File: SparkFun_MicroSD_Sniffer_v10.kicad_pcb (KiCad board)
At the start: 16 copper layers, 47 x 27.9 mm, 9 parts, among them U1 MICRO-SDCARD

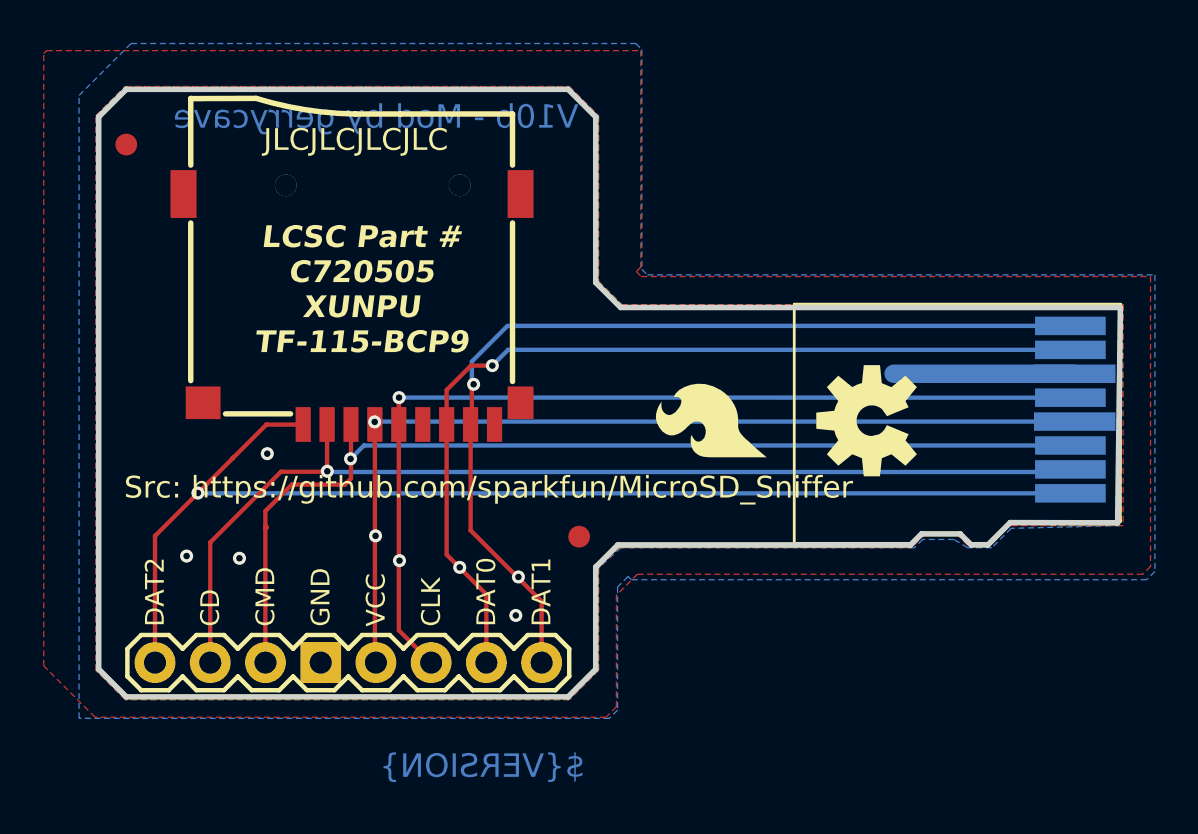
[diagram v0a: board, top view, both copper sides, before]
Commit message: Add silkscreen to increase height in the uSD section
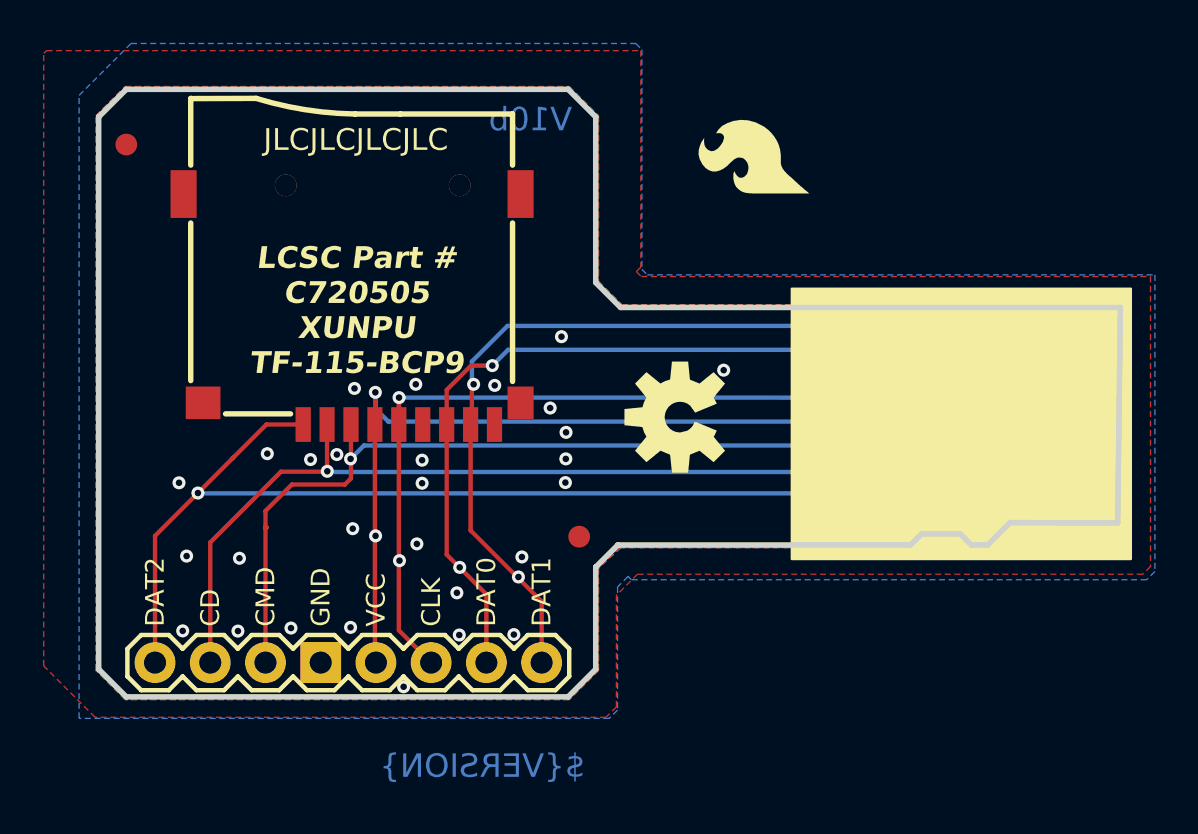
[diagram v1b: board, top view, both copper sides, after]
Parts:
- moved LOGO2 12.3 mm to (158.0, 96.2)
- moved LOGO3 11.3 mm to (142.2, 88.5)
- moved LOGO1 8.82 mm to (151.7, 106.1)
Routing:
- net VCC: track 43.3 -> 45.8 mm
- net GND: vias 4 -> 28
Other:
- board text added: "V10b"
- board text removed: "V10b - Mod by gerrycave"
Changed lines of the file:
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@@
   )
   (footprint "SparkFun_MicroSD_Sniffer_v10:OSHW-LOGO-M" (layer "F.Cu")
-    (at 160.5661 106.2736 90)
+    (at 151.742727 106.11 90)
     (property "Sheetfile" "SparkFun_MicroSD_Sniffer_v10.kicad_sch")
     (property "Sheetname" "")
@@
   )
   (footprint "SparkFun_MicroSD_Sniffer_v10:SFE_LOGO_FLAME_.2" (layer "F.Cu")
-    (at 155.9941 108.3056 90)
+    (at 157.956277 96.171276 90)
     (property "Sheetfile" "SparkFun_MicroSD_Sniffer_v10.kicad_sch")
     (property "Sheetname" "")
@@
   )
   (footprint "SparkFun_MicroSD_Sniffer_v10:SFE_LOGO_NAME_FLAME_.1" (layer "B.Cu")
-    (at 143.55127 99.74127 180)
+    (at 142.18127 88.49127 180)
     (property "Sheetfile" "SparkFun_MicroSD_Sniffer_v10.kicad_sch")
     (property "Sheetname" "")
@@
       (stroke (width 0) (type default)) (fill solid) (layer "B.SilkS"))
   )
+  (gr_rect (start 156.88 100.2) (end 172.48 112.64)
+    (stroke (width 0.1) (type solid)) (fill solid) (layer "F.SilkS"))
   (gr_line (start 164.6301 111.4806) (end 162.8521 111.4806)
     (stroke (width 0.254) (type solid)) (layer "Edge.Cuts"))
@@
   (gr_line (start 125.0061 92.3036) (end 126.2761 91.0336)
     (stroke (width 0.254) (type solid)) (layer "Edge.Cuts"))
-  (gr_text "V10b - Mod by gerrycave" (at 147.08 92.93) (layer "B.Cu")
+  (gr_text "V10b" (at 146.78 93.05) (layer "B.Cu")
     (effects (font (size 1.0795 1.0795) (thickness 0.1905)) (justify left bottom mirror))
+  )
+  (gr_text "Src: https://github.com/sparkfun/MicroSD_Sniffer" (at 156.4 104.31) (layer "B.SilkS")
+    (effects (font (size 0.8 0.8) (thickness 0.1)) (justify left bottom mirror))
   )
   (gr_text "GND" (at 134.7343 115.7478 -90) (layer "B.SilkS")
@@
     (effects (font (size 0.8636 0.8636) (thickness 0.1524)) (justify left bottom))
   )
-  (gr_text "Src: https://github.com/sparkfun/MicroSD_Sniffer" (at 126.17 109.93) (layer "F.SilkS")
-    (effects (font (size 1 1) (thickness 0.1)) (justify left bottom))
-  )
   (gr_text "DAT2" (at 128.1049 115.7478 90) (layer "F.SilkS")
     (effects (font (size 0.8636 0.8636) (thickness 0.1524)) (justify left bottom))
@@
     (effects (font (size 0.8636 0.8636) (thickness 0.1524)) (justify left bottom))
   )
-  (gr_text "LCSC Part #\nC720505\nXUNPU\nTF-115-BCP9" (at 137.09 103.24) (layer "F.SilkS")
+  (gr_text "LCSC Part #\nC720505\nXUNPU\nTF-115-BCP9" (at 136.87 104.2) (layer "F.SilkS")
     (effects (font (size 1 1) (thickness 0.2) bold italic) (justify bottom))
   )
@@
     (effects (font (size 1.6002 1.6002) (thickness 0.1778)) (justify left bottom))
   )
+  (via (at 134.75 108.06) (size 0.6) (drill 0.3) (layers "F.Cu" "B.Cu") (free) (net 1))
+  (via (at 128.7 109.13) (size 0.6) (drill 0.3) (layers "F.Cu" "B.Cu") (free) (net 1))
+  (via (at 139.03 118.51) (size 0.6) (drill 0.3) (layers "F.Cu" "B.Cu") (free) (net 1))
+  (via (at 128.87 115.94) (size 0.6) (drill 0.3) (layers "F.Cu" "B.Cu") (free) (net 1))
+  (via (at 141.59 116.13) (size 0.6) (drill 0.3) (layers "F.Cu" "B.Cu") (free) (net 1))
+  (via (at 139.59 104.6) (size 0.6) (drill 0.3) (layers "F.Cu" "B.Cu") (free) (net 1))
+  (via (at 141.48 114.19) (size 0.6) (drill 0.3) (layers "F.Cu" "B.Cu") (free) (net 1))
+  (via (at 146.29 102.41) (size 0.6) (drill 0.3) (layers "F.Cu" "B.Cu") (free) (net 1))
+  (via (at 146.5 106.81) (size 0.6) (drill 0.3) (layers "F.Cu" "B.Cu") (free) (net 1))
+  (via (at 136.69 111.24) (size 0.6) (drill 0.3) (layers "F.Cu" "B.Cu") (free) (net 1))
   (via (at 129.05 112.5) (size 0.6) (drill 0.3) (layers "F.Cu" "B.Cu") (free) (net 1))
   (via (at 132.76 107.79) (size 0.6) (drill 0.3) (layers "F.Cu" "B.Cu") (free) (net 1))
-  (via (at 144.19 115.23) (size 0.6) (drill 0.3) (layers "F.Cu" "B.Cu") (free) (net 1))
+  (via (at 139.88 109.15) (size 0.6) (drill 0.3) (layers "F.Cu" "B.Cu") (free) (net 1))
+  (via (at 144.1 116.11) (size 0.6) (drill 0.3) (layers "F.Cu" "B.Cu") (free) (net 1))
+  (via (at 153.75 103.95) (size 0.6) (drill 0.3) (layers "F.Cu" "B.Cu") (free) (net 1))
+  (via (at 139.88 108.09) (size 0.6) (drill 0.3) (layers "F.Cu" "B.Cu") (free) (net 1))
+  (via (at 133.85 115.81) (size 0.6) (drill 0.3) (layers "F.Cu" "B.Cu") (free) (net 1))
+  (via (at 146.49 108.03) (size 0.6) (drill 0.3) (layers "F.Cu" "B.Cu") (free) (net 1))
+  (via (at 131.41 115.95) (size 0.6) (drill 0.3) (layers "F.Cu" "B.Cu") (free) (net 1))
   (via (at 131.48 112.6) (size 0.6) (drill 0.3) (layers "F.Cu" "B.Cu") (free) (net 1))
+  (via (at 139.64 111.94) (size 0.6) (drill 0.3) (layers "F.Cu" "B.Cu") (free) (net 1))
+  (via (at 146.47 109.12) (size 0.6) (drill 0.3) (layers "F.Cu" "B.Cu") (free) (net 1))
+  (via (at 145.77 105.69) (size 0.6) (drill 0.3) (layers "F.Cu" "B.Cu") (free) (net 1))
+  (via (at 135.96 107.83) (size 0.6) (drill 0.3) (layers "F.Cu" "B.Cu") (free) (net 1))
+  (via (at 144.47 112.54) (size 0.6) (drill 0.3) (layers "F.Cu" "B.Cu") (free) (net 1))
+  (via (at 136.77 104.79) (size 0.6) (drill 0.3) (layers "F.Cu" "B.Cu") (free) (net 1))
+  (via (at 143.22 104.65) (size 0.6) (drill 0.3) (layers "F.Cu" "B.Cu") (free) (net 1))
+  (via (at 136.59 115.78) (size 0.6) (drill 0.3) (layers "F.Cu" "B.Cu") (free) (net 1))
   (segment locked (start 161.5658 104.1142) (end 169.8961 104.1142) (width 0.85) (layer "B.Cu") (net 1))
   (segment (start 137.71 106.34) (end 137.71 106.45) (width 0.2) (layer "F.Cu") (net 2))
@@
   (segment (start 137.7569 117.3988) (end 137.71 117.3519) (width 0.2) (layer "F.Cu") (net 2))
   (segment (start 137.74 111.57) (end 137.71 111.54) (width 0.2) (layer "F.Cu") (net 2))
+  (segment (start 137.73 106.43) (end 137.71 106.45) (width 0.2) (layer "F.Cu") (net 2))
   (segment (start 137.7 106.33) (end 137.71 106.34) (width 0.2) (layer "F.Cu") (net 2))
   (segment (start 137.71 117.3519) (end 137.71 111.6) (width 0.2) (layer "F.Cu") (net 2))
   (segment (start 137.71 111.6) (end 137.74 111.57) (width 0.2) (layer "F.Cu") (net 2))
   (segment (start 137.71 106.32) (end 137.7 106.33) (width 0.2) (layer "F.Cu") (net 2))
-  (via (at 137.7 106.33) (size 0.6) (drill 0.3) (layers "F.Cu" "B.Cu") (net 2))
+  (segment (start 137.73 104.97) (end 137.73 106.43) (width 0.2) (layer "F.Cu") (net 2))
+  (via (at 137.73 104.97) (size 0.6) (drill 0.3) (layers "F.Cu" "B.Cu") (net 2))
   (via (at 137.74 111.57) (size 0.6) (drill 0.3) (layers "F.Cu" "B.Cu") (net 2))
-  (segment (start 137.7 106.33) (end 137.7158 106.3142) (width 0.2) (layer "B.Cu") (net 2))
-  (segment (start 137.7158 106.3142) (end 169.8961 106.3142) (width 0.2) (layer "B.Cu") (net 2))
+  (segment (start 137.73 104.97) (end 137.73 105.7142) (width 0.2) (layer "B.Cu") (net 2))
+  (segment (start 137.73 105.7142) (end 138.33 106.3142) (width 0.2) (layer "B.Cu") (net 2))
+  (segment (start 138.33 106.3142) (end 169.8961 106.3142) (width 0.2) (layer "B.Cu") (net 2))
   (segment (start 129.57 109.6) (end 131.17 108) (width 0.2) (layer "F.Cu") (net 3))
   (segment (start 131.19 107.98) (end 132.72 106.45) (width 0.2) (layer "F.Cu") (net 3))
